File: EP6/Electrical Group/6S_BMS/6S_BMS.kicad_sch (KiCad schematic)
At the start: 16 parts, among them J1 BATcellMain, J10 CAN1, J11 frontBox, J13 RESET, J14 battery cells, J2 BAT charge, J3 GLVMS, J4 24Vout, J6 UART2, J7 I2C1, J8 7seg, J9 SWD

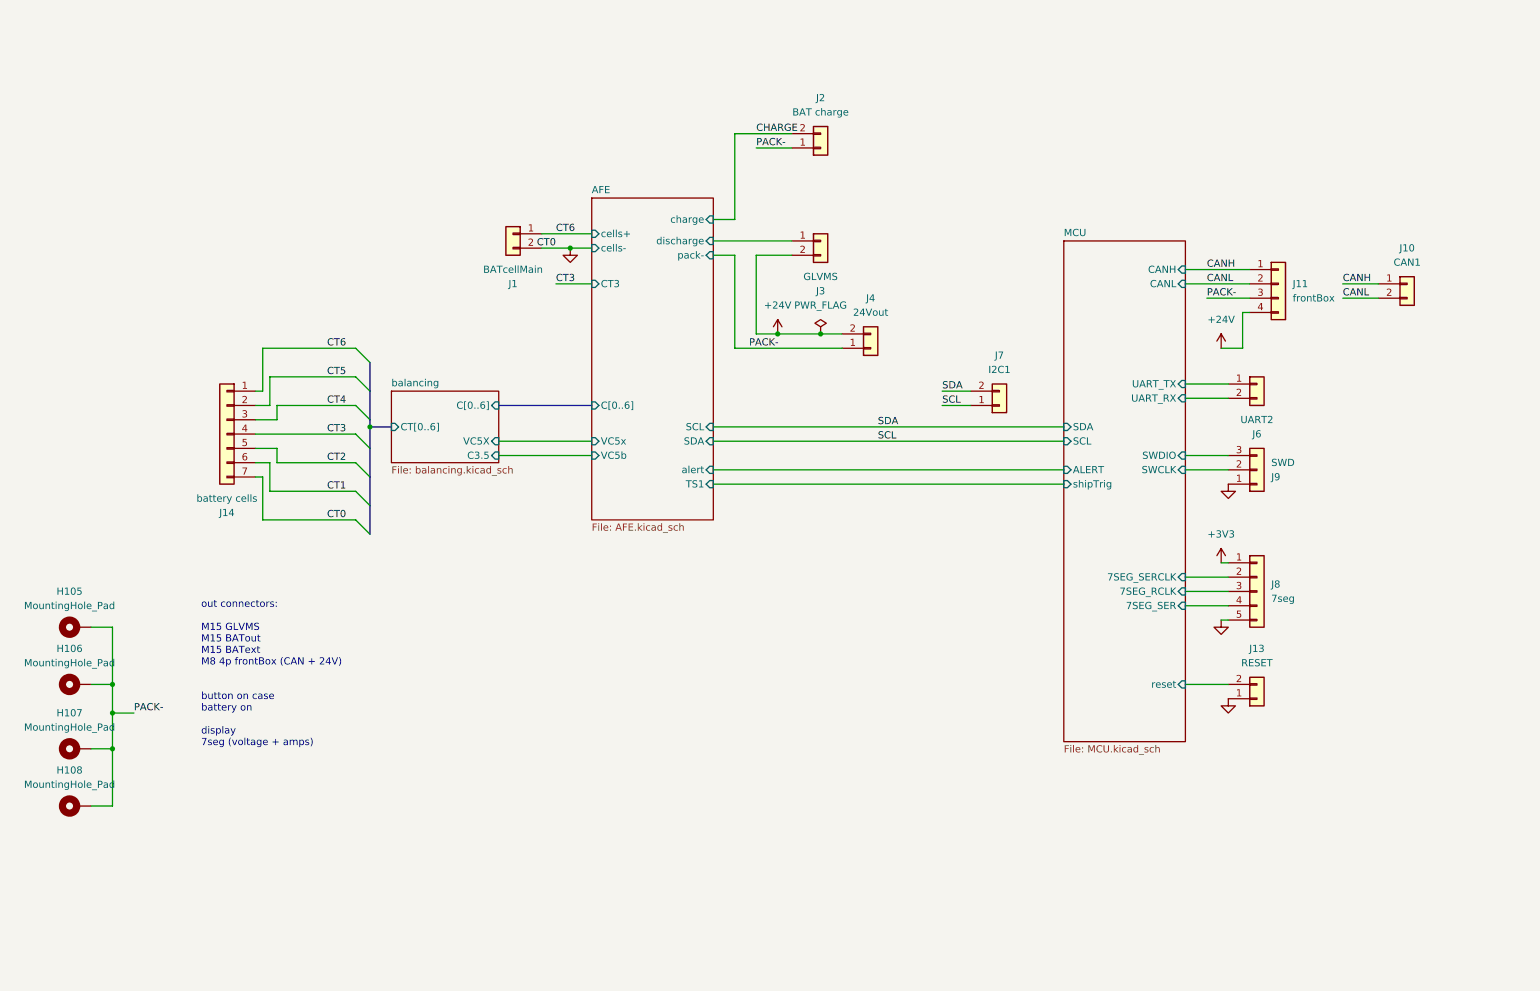
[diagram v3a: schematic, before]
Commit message: 6S BMS sch cleanup
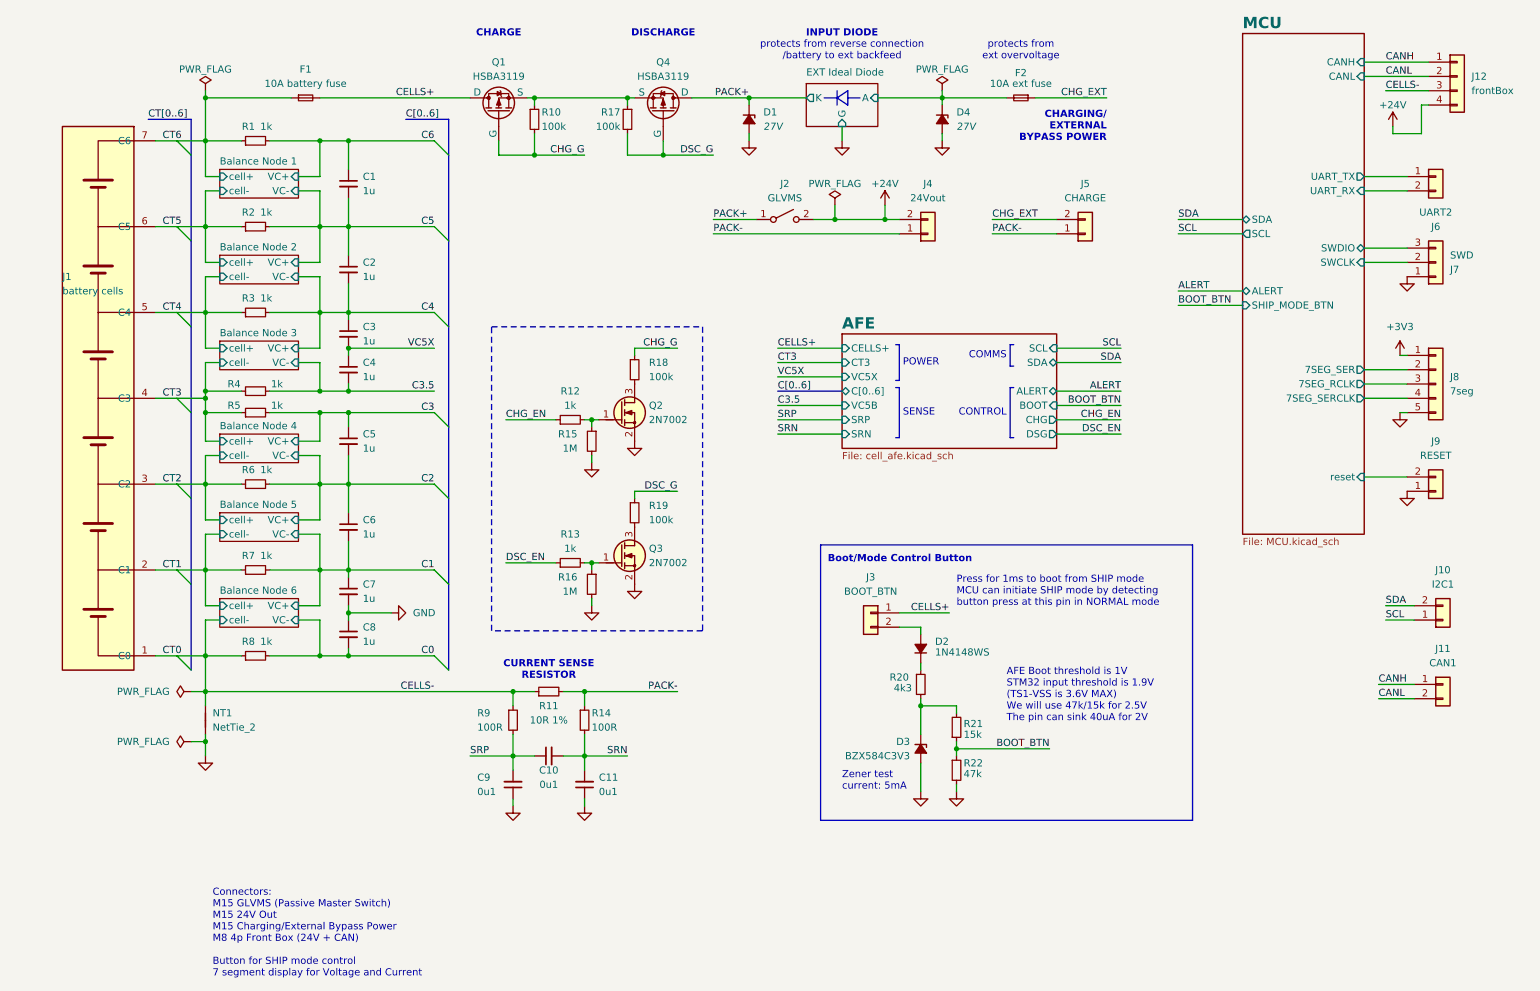
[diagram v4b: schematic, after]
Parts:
- removed H105, H106, H107, H108: MountingHole_Pad, MountingHole:MountingHole_3.2mm_M3_Pad_TopBottom, symbol Mechanical:MountingHole_Pad
- removed J1: BATcellMain, Connector_AMASS:AMASS_XT60PW-M_1x02_P7.20mm_Horizontal, symbol Connector_Generic:Conn_01x02
- removed J2: BAT charge, Connector_AMASS:AMASS_XT60PW-M_1x02_P7.20mm_Horizontal, symbol Connector_Generic:Conn_01x02
- added C1, C2, C3, C4, C5, C6, C7, C8: 1u, Capacitor_SMD:C_0402_1005Metric, symbol Device:C_Small
- added C10, C11, C9: 0u1, Capacitor_SMD:C_0402_1005Metric, symbol Device:C_Small
- added D1, D4: 27V, Diode_SMD:D_SOD-123, symbol Device:D_Zener_Small_Filled
- added D2: 1N4148WS, Diode_SMD:D_SOD-323, symbol Device:D_Small_Filled
- added D3: BZX584C3V3, Diode_SMD:D_SOD-323, symbol Device:D_Zener_Small_Filled
- added F1: 10A battery fuse, Fuse:Fuseholder_Cylinder-5x20mm_Schurter_0031_8201_Horizontal_Open, symbol Device:Fuse_Small
- added F2: 10A ext fuse, Fuse:Fuseholder_Cylinder-5x20mm_Schurter_0031_8201_Horizontal_Open, symbol Device:Fuse_Small
- added J2: GLVMS, Connector_JST:JST_VH_B2PS-VH_1x02_P3.96mm_Horizontal, symbol Switch:SW_SPST
- added J5: CHARGE, Connector_AMASS:AMASS_XT60PW-M_1x02_P7.20mm_Horizontal, symbol Connector_Generic:Conn_01x02
- added NT1: NetTie_2, symbol Device:NetTie_2
- added Q1, Q4: HSBA3119, nturt_kicad_lib_EP6:HSBA3119_PRPAK5X6, symbol nturt_kicad_lib_EP6:HSBA3119_PMOS_GSDnumber
- added Q2, Q3: 2N7002, PCM_Package_TO_SOT_SMD_AKL:SOT-23, symbol PCM_Transistor_MOSFET_AKL:2N7002
- added R1, R2, R3, R4, R5, R6, R7, R8: 1k, symbol Device:R_Small
- added R10, R17, R18, R19: 100k, Resistor_SMD:R_0402_1005Metric, symbol Device:R_Small
- added R11: 10R 1%, Resistor_SMD:R_0805_2012Metric, symbol Device:R_Small
- added R12, R13: 1k, Resistor_SMD:R_0402_1005Metric, symbol Device:R_Small
- added R14, R9: 100R, Resistor_SMD:R_0402_1005Metric, symbol Device:R_Small
- added R15, R16: 1M, Resistor_SMD:R_0402_1005Metric, symbol Device:R_Small
- added R20: 4k3, Resistor_SMD:R_0402_1005Metric, symbol Device:R_Small
- added R21: 15k, Resistor_SMD:R_0402_1005Metric, symbol Device:R_Small
- added R22: 47k, Resistor_SMD:R_0402_1005Metric, symbol Device:R_Small
- J1: renamed from J14; symbol Connector_Generic:Conn_01x07 -> nturt_kicad_lib:6S_Battery
- J3: value GLVMS -> BOOT_BTN; footprint Connector_JST:JST_VH_B2PS-VH_1x02_P3.96mm_Horizontal -> Connector_JST:JST_XH_S2B-XH-A_1x02_P2.50mm_Horizontal
- renumbered J7 to J10, J10 to J11, J11 to J12, J9 to J7, J13 to J9
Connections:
- net +24V: now also J2.2 (B); no longer J3.2 (Pin_2)
- net CT1: now also J1.2 (C1), R7.1; no longer J1.6 (Pin_6)
- net CT2: now also J1.3 (C2), R6.1; no longer J1.5 (Pin_5)
- net CT3: now also R4.1, R5.1
- net CT4: now also J1.5 (C4), R3.1; no longer J1.3 (Pin_3)
- net CT5: now also J1.6 (C5), R2.1; no longer J1.2 (Pin_2)
- net CT6: now also J1.7 (C6), F1.1, R1.1; no longer J1.1 (Pin_1)
- net GND: now also C11.1, C7.2, C8.1, C9.1, D1.2 (A), D3.2 (A), D4.2 (A), NT1.1, Q2.2 (S), Q3.2 (S), R15.2, R16.2, R22.2; no longer J1.7 (Pin_7)
- net MCU/7SEG_SER: now also J8.2 (Pin_2); no longer J8.4 (Pin_4)
- net MCU/7SEG_SERCLK: now also J8.4 (Pin_4); no longer J8.2 (Pin_2)
- net PACK-: now also J5.1 (Pin_1), R11.2, R14.1; no longer J12.3 (Pin_3)
- net AFE/discharge renamed CELLS+
- net CELLS+: now also F1.2, Q1.D
- new net: Q1.S, Q4.S, R10.1, R17.1
- new net: D2.1 (K), R20.1
- new net: D3.1 (K), R20.2, R21.2
- new net: Q2.3 (D), R18.2
- new net: Q3.3 (D), R19.2
- new net: Q2.1 (G), R12.2, R15.1
- new net: Q3.1 (G), R13.2, R16.1
- new net: D2.2 (A), J3.2 (Pin_2)
- new net BOOT_BTN: R21.1, R22.1
- new net C0: C8.2, R8.2
- new net C1: C6.2, C7.1, R7.2
- new net C2: C5.2, C6.1, R6.2
- new net C3: C5.1, R5.2
- new net C3.5: C4.2, R4.2
- new net C4: C2.2, C3.1, R3.2
- new net C5: C1.2, C2.1, R2.2
- new net C6: C1.1, R1.2
- new net CELLS-: J1.1 (C0), J12.3 (Pin_3), NT1.2, R11.1, R8.1, R9.1
- new net CHG_EN: R12.1
- new net CHG_EXT: F2.1, J5.2 (Pin_2)
- new net CHG_G: Q1.G, R10.2, R18.1
- new net DSC_EN: R13.1
- new net DSC_G: Q4.G, R17.2, R19.1
- new net EXT Ideal Diode/A: D4.1 (K), F2.2
- new net PACK+: D1.1 (K), J2.1 (A), Q4.D
- new net SRN: C10.2, C11.2, R14.2
- new net SRP: C10.1, C9.2, R9.2
- new net VC5X: C3.2, C4.1
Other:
- removed sheet balancing
- added sheet Balance Node 1 (balance_node_1.kicad_sch)
- added sheet Balance Node 2 (balance_node_1.kicad_sch)
- added sheet Balance Node 3 (balance_node_1.kicad_sch)
- added sheet Balance Node 4 (balance_node_1.kicad_sch)
- added sheet Balance Node 5 (balance_node_1.kicad_sch)
- added sheet Balance Node 6 (balance_node_1.kicad_sch)
- added sheet EXT Ideal Diode (ext_ideal_diode.kicad_sch)
- sheet AFE: file AFE.kicad_sch -> cell_afe.kicad_sch
- sheet AFE ports: added ALERT, BOOT, CELLS+, CHG, DSG, SRN, SRP, VC5B, VC5X; removed TS1, VC5b, VC5x, alert, cells+, cells-, charge, discharge, pack-
- sheet MCU ports: added SHIP_MODE_BTN; removed shipTrig
- note added: "AFE Boot threshold is 1V STM32 input threshold is 1.9V (TS1-VSS is 3.6V MAX) We will use 47k/15k for 2.5V The pin can sink 40uA for 2V"
- note added: "Boot/Mode Control Button"
- note added: "CHARGE"
- note added: "CHARGING/ EXTERNAL BYPASS POWER"
- note added: "COMMS"
- note added: "CONTROL"
- note added: "CURRENT SENSE RESISTOR"
- note added: "Connectors: M15 GLVMS (Passive Master Switch) M15 24V Out M15 Charging/External Bypass Power M8 4p Front Box (24V + CAN) Button for SHIP mode control 7 segment display for Voltage and Current"
- note added: "DISCHARGE"
- note added: "INPUT DIODE"
- note added: "POWER"
- note added: "Press for 1ms to boot from SHIP mode MCU can initiate SHIP mode by detecting button press at this pin in NORMAL mode"
- note added: "SENSE"
- note added: "Zener test current: 5mA"
- note added: "protects from ext overvoltage"
- note added: "protects from reverse connection /battery to ext backfeed"
- note removed: "out connectors: M15 GLVMS M15 BATout M15 BAText M8 4p frontBox (CAN + 24V) button on case battery on display 7seg (voltage + amps)"
- moved on the sheet: J10, J11, J12, J6, J7, J8, J9

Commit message: fix library
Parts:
- J1: symbol nturt_kicad_lib:6S_Battery -> nturt_kicad_lib_EP6:6S_Battery
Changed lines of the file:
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@@
 	)
 	(symbol
-		(lib_id "nturt_kicad_lib:6S_Battery")
+		(lib_id "nturt_kicad_lib_EP6:6S_Battery")
 		(at 27.94 107.95 0)
 		(mirror y)

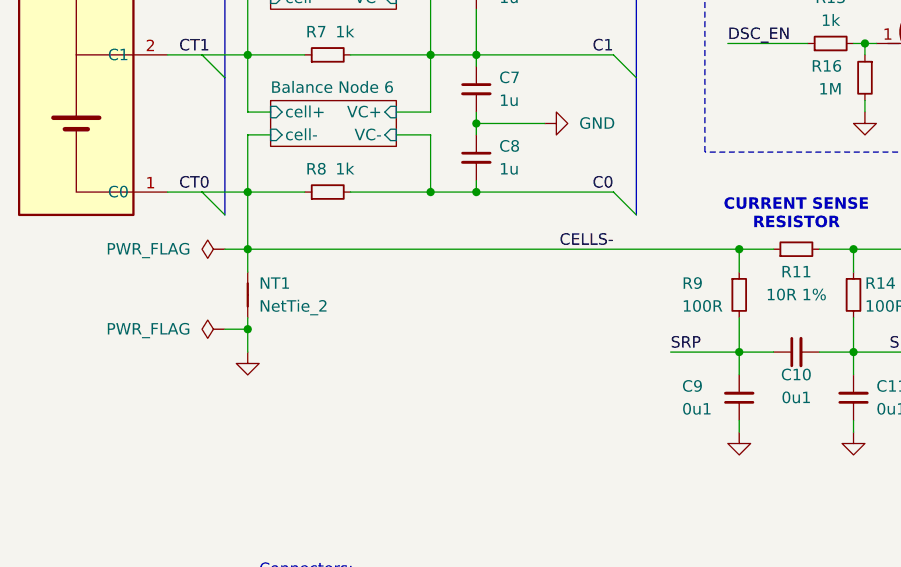
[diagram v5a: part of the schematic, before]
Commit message: fix net ties
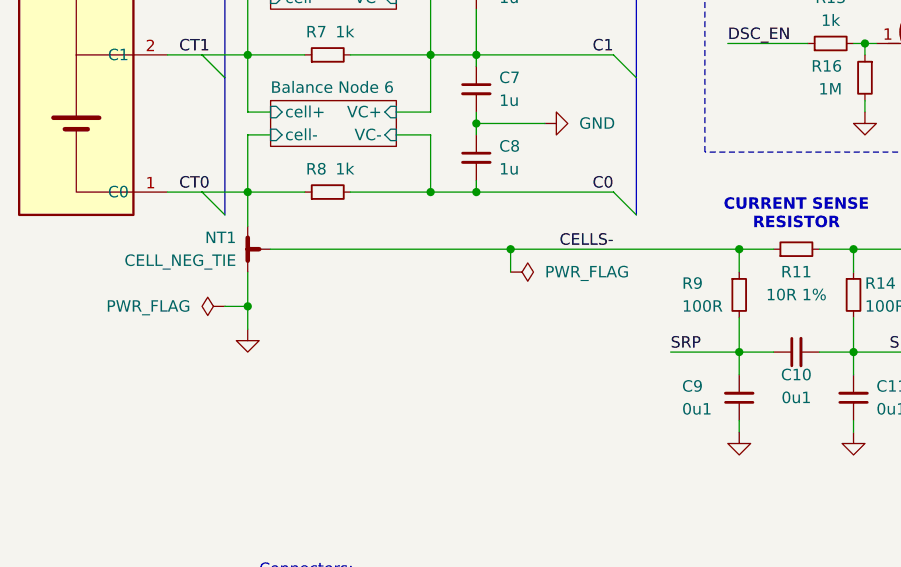
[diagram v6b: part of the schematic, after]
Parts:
- removed NT1: NetTie_2, symbol Device:NetTie_2
- added NT1: CELL_NEG_TIE, symbol Device:NetTie_3_Tee
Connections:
- net CELLS-: now also NT1.3; no longer J1.1 (C0), R8.1
- net GND: now also NT1.1
- new net CT0: J1.1 (C0), NT1.2, R8.1

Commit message: added nickel tabs footprint, assigned footprints
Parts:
- J1: footprint Connector_JST:JST_XH_S7B-XH-A_1x07_P2.50mm_Horizontal -> nturt_kicad_lib_EP6:6S_batteries_100mm_across
- J10, J3, J6, J9: footprint Connector_JST:JST_XH_S2B-XH-A_1x02_P2.50mm_Horizontal -> Connector_JST:JST_PH_S2B-PH-K_1x02_P2.00mm_Horizontal
- J11: footprint Connector_JST:JST_XH_B2B-XH-A_1x02_P2.50mm_Vertical -> Connector_JST:JST_PH_S2B-PH-K_1x02_P2.00mm_Horizontal
- J12: footprint Connector_JST:JST_XH_S4B-XH-A_1x04_P2.50mm_Horizontal -> Connector_JST:JST_PH_S4B-PH-K_1x04_P2.00mm_Horizontal
- J2: footprint Connector_JST:JST_VH_B2PS-VH_1x02_P3.96mm_Horizontal -> Connector_JST:JST_PH_S2B-PH-K_1x02_P2.00mm_Horizontal
- J7: footprint Connector_JST:JST_XH_S3B-XH-A_1x03_P2.50mm_Horizontal -> Connector_JST:JST_PH_S3B-PH-K_1x03_P2.00mm_Horizontal
- J8: footprint Connector_JST:JST_XH_S5B-XH-A_1x05_P2.50mm_Horizontal -> Connector_JST:JST_PH_S5B-PH-K_1x05_P2.00mm_Horizontal
- NT1: footprint (none) -> NetTie:NetTie-3_SMD_Pad0.5mm
- Q2, Q3: footprint PCM_Package_TO_SOT_SMD_AKL:SOT-23 -> Package_TO_SOT_SMD:SOT-23
- R1, R2, R3, R4, R5, R6, R7, R8: footprint (none) -> Resistor_SMD:R_0402_1005Metric
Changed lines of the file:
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@@
 			)
 		)
-		(property "Footprint" ""
+		(property "Footprint" "NetTie:NetTie-3_SMD_Pad0.5mm"
 			(at 46.99 137.16 0)
 			(effects
@@
 			)
 		)
-		(property "Footprint" "Connector_JST:JST_XH_S4B-XH-A_1x04_P2.50mm_Horizontal"
+		(property "Footprint" "Connector_JST:JST_PH_S4B-PH-K_1x04_P2.00mm_Horizontal"
 			(at 269.24 27.94 0)
 			(effects
@@
 			)
 		)
-		(property "Footprint" ""
+		(property "Footprint" "Resistor_SMD:R_0402_1005Metric"
 			(at 55.88 69.85 0)
 			(effects
@@
 			)
 		)
-		(property "Footprint" ""
+		(property "Footprint" "Resistor_SMD:R_0402_1005Metric"
 			(at 55.88 130.81 0)
 			(effects
@@
 			)
 		)
-		(property "Footprint" ""
+		(property "Footprint" "Resistor_SMD:R_0402_1005Metric"
 			(at 55.88 115.57 0)
 			(effects
@@
 			)
 		)
-		(property "Footprint" "Connector_JST:JST_XH_B2B-XH-A_1x02_P2.50mm_Vertical"
+		(property "Footprint" "Connector_JST:JST_PH_S2B-PH-K_1x02_P2.00mm_Horizontal"
 			(at 266.7 135.89 0)
 			(effects
@@
 			)
 		)
-		(property "Footprint" "Connector_JST:JST_XH_S2B-XH-A_1x02_P2.50mm_Horizontal"
+		(property "Footprint" "Connector_JST:JST_PH_S2B-PH-K_1x02_P2.00mm_Horizontal"
 			(at 265.43 45.72 0)
 			(effects
@@
 			)
 		)
-		(property "Footprint" "Connector_JST:JST_XH_S7B-XH-A_1x07_P2.50mm_Horizontal"
+		(property "Footprint" "nturt_kicad_lib_EP6:6S_batteries_100mm_across"
 			(at 27.94 107.95 0)
 			(effects
@@
 			)
 		)
-		(property "Footprint" "PCM_Package_TO_SOT_SMD_AKL:SOT-23"
+		(property "Footprint" "Package_TO_SOT_SMD:SOT-23"
 			(at 125.73 85.09 0)
 			(effects
@@
 			)
 		)
-		(property "Footprint" "Connector_JST:JST_XH_S2B-XH-A_1x02_P2.50mm_Horizontal"
+		(property "Footprint" "Connector_JST:JST_PH_S2B-PH-K_1x02_P2.00mm_Horizontal"
 			(at 265.43 101.6 0)
 			(effects
@@
 			)
 		)
-		(property "Footprint" ""
+		(property "Footprint" "Resistor_SMD:R_0402_1005Metric"
 			(at 55.88 100.33 0)
 			(effects
@@
 			)
 		)
-		(property "Footprint" "Connector_JST:JST_XH_S2B-XH-A_1x02_P2.50mm_Horizontal"
+		(property "Footprint" "Connector_JST:JST_PH_S2B-PH-K_1x02_P2.00mm_Horizontal"
 			(at 165.1 123.19 0)
 			(effects
@@
 			)
 		)
-		(property "Footprint" "Connector_JST:JST_XH_S5B-XH-A_1x05_P2.50mm_Horizontal"
+		(property "Footprint" "Connector_JST:JST_PH_S5B-PH-K_1x05_P2.00mm_Horizontal"
 			(at 265.43 82.55 0)
 			(effects
@@
 			)
 		)
-		(property "Footprint" "Connector_JST:JST_XH_S2B-XH-A_1x02_P2.50mm_Horizontal"
+		(property "Footprint" "Connector_JST:JST_PH_S2B-PH-K_1x02_P2.00mm_Horizontal"
 			(at 266.7 124.46 0)
 			(effects
@@
 			)
 		)
-		(property "Footprint" ""
+		(property "Footprint" "Resistor_SMD:R_0402_1005Metric"
 			(at 55.88 54.61 0)
 			(effects
@@
 			)
 		)
-		(property "Footprint" "PCM_Package_TO_SOT_SMD_AKL:SOT-23"
+		(property "Footprint" "Package_TO_SOT_SMD:SOT-23"
 			(at 125.73 110.49 0)
 			(effects
@@
 			)
 		)
-		(property "Footprint" "Connector_JST:JST_VH_B2PS-VH_1x02_P3.96mm_Horizontal"
+		(property "Footprint" "Connector_JST:JST_PH_S2B-PH-K_1x02_P2.00mm_Horizontal"
 			(at 149.86 53.34 0)
 			(effects
@@
 			)
 		)
-		(property "Footprint" ""
+		(property "Footprint" "Resistor_SMD:R_0402_1005Metric"
 			(at 55.88 39.37 0)
 			(effects
@@
 			)
 		)
-		(property "Footprint" ""
+		(property "Footprint" "Resistor_SMD:R_0402_1005Metric"
 			(at 55.88 87.63 0)
 			(effects
@@
 			)
 		)
-		(property "Footprint" ""
+		(property "Footprint" "Resistor_SMD:R_0402_1005Metric"
 			(at 55.88 83.82 0)
 			(effects
@@
 			)
 		)
-		(property "Footprint" "Connector_JST:JST_XH_S3B-XH-A_1x03_P2.50mm_Horizontal"
+		(property "Footprint" "Connector_JST:JST_PH_S3B-PH-K_1x03_P2.00mm_Horizontal"
 			(at 265.43 60.96 0)
 			(effects
